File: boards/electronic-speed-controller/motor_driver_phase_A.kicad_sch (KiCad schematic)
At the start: 18 parts, among them U2 MIC4605-2YM-TR, U3 SISHA14DN-T1-GE3, U4 SISHA14DN-T1-GE3, U5 INA180A3IDBVR

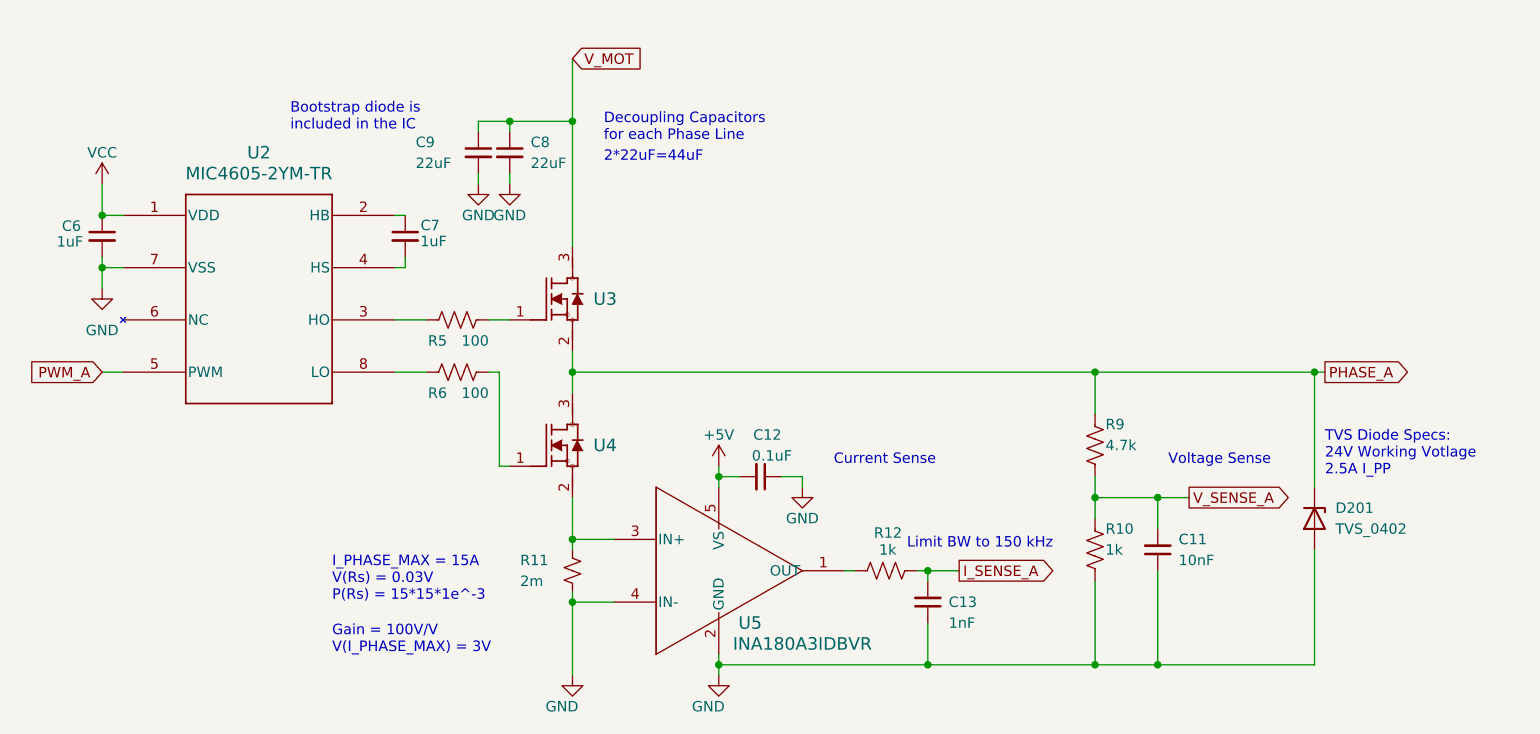
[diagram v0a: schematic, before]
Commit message: updated MOSFETs
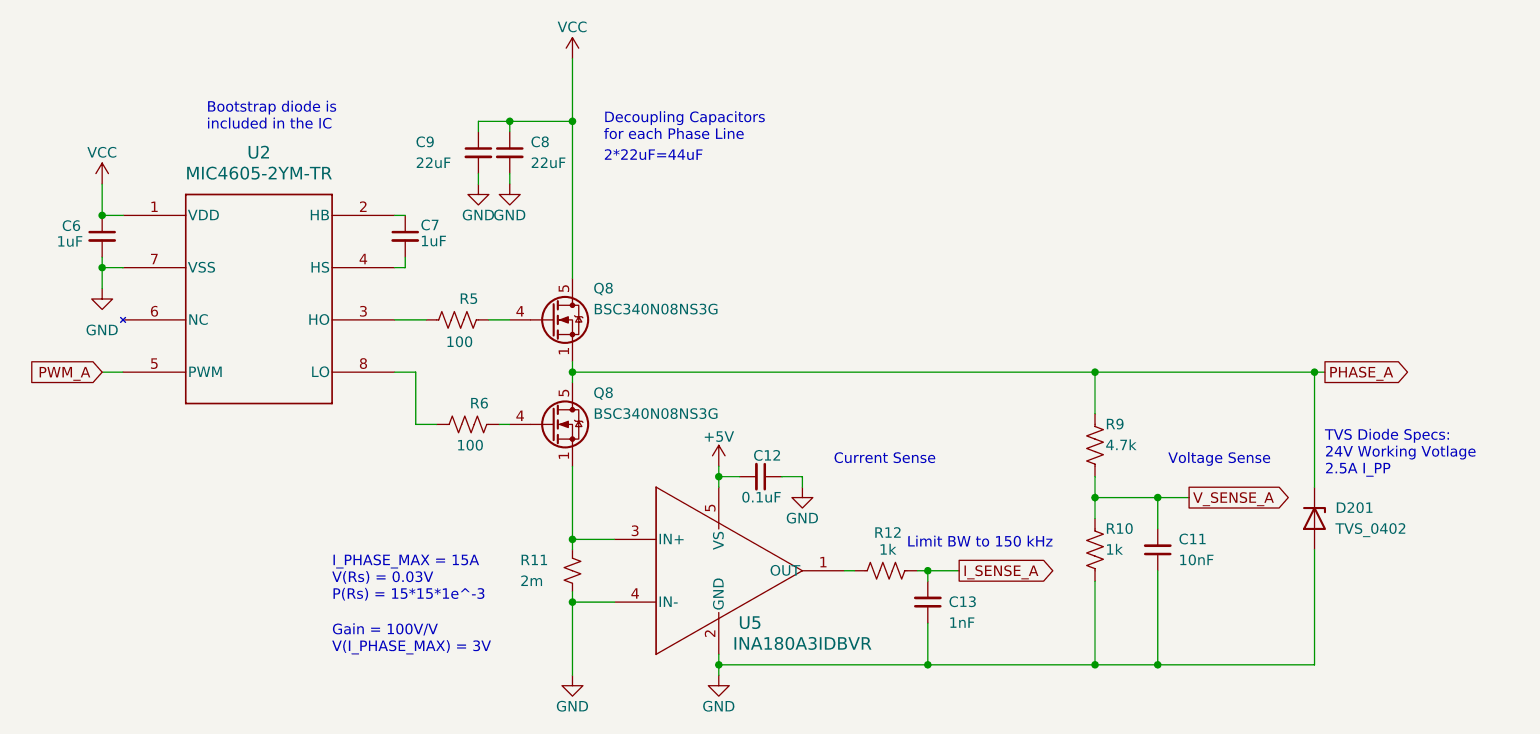
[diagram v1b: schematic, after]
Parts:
- removed U3, U4: SISHA14DN-T1-GE3, MOSFET_3DN-T1-GE3_VIS, symbol N-Channel MOSFET:SISHA14DN-T1-GE3
- added Q8 (x2): BSC340N08NS3G, Package_TO_SOT_SMD:TDSON-8-1, symbol Transistor_FET:BSC340N08NS3G
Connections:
- net V_MOT is gone; now on net VCC: C8.1, C9.1
- net PHASE_A: now also Q8.1 (S), Q8.2 (S), Q8.3 (S), Q8.5 (D)
- net VCC: now also Q8.5 (D)
- net at R6.2: now also Q8.4 (G)
- net at R11.1, U5.3 (IN+): now also Q8.1 (S), Q8.2 (S), Q8.3 (S)
- net at R5.2: now also Q8.4 (G)
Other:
- moved on the sheet: R6

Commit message: simplified PHASE A circuit
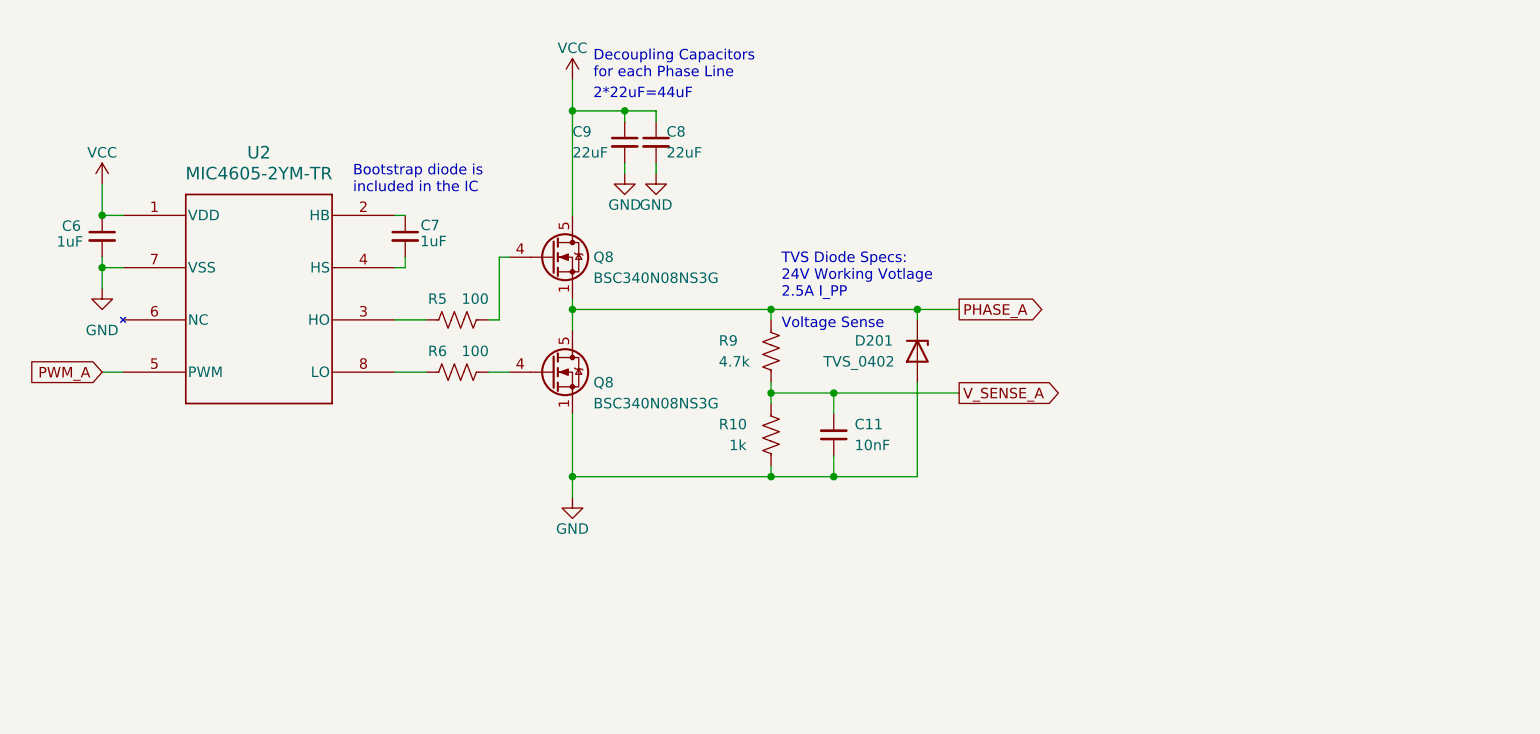
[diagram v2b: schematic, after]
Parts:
- removed C12: 0.1uF, Capacitor_SMD:C_0603_1608Metric, symbol Device:C_Small
- removed C13: 1nF, Capacitor_SMD:C_0603_1608Metric, symbol Device:C_Small
- removed R11: 2m, Resistor_SMD:R_2512_6332Metric, symbol Device:R_Small_US
- removed R12: 1k, Resistor_SMD:R_0603_1608Metric, symbol Device:R_US
- removed U5: INA180A3IDBVR, DBV0005A_N, symbol Current_Sense_Amp:INA180A3IDBVR
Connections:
- net GND: now also Q8.1 (S), Q8.2 (S), Q8.3 (S)
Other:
- note removed: "Current Sense"
- note removed: "Gain = 100V/V V(I_PHASE_MAX) = 3V"
- note removed: "I_PHASE_MAX = 15A V(Rs) = 0.03V P(Rs) = 15*15*1e^-3"
- note removed: "Limit BW to 150 kHz"
- moved on the sheet: C11, C8, C9, D201, Q8, R10, R6, R9
